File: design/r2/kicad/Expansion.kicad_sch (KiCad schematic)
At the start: 29 parts, among them IC1 MC68010P10, IC7 74LS148, J3 Conn_02x32_Odd_Even, J5 PWR, J6 Conn_01x04_Male

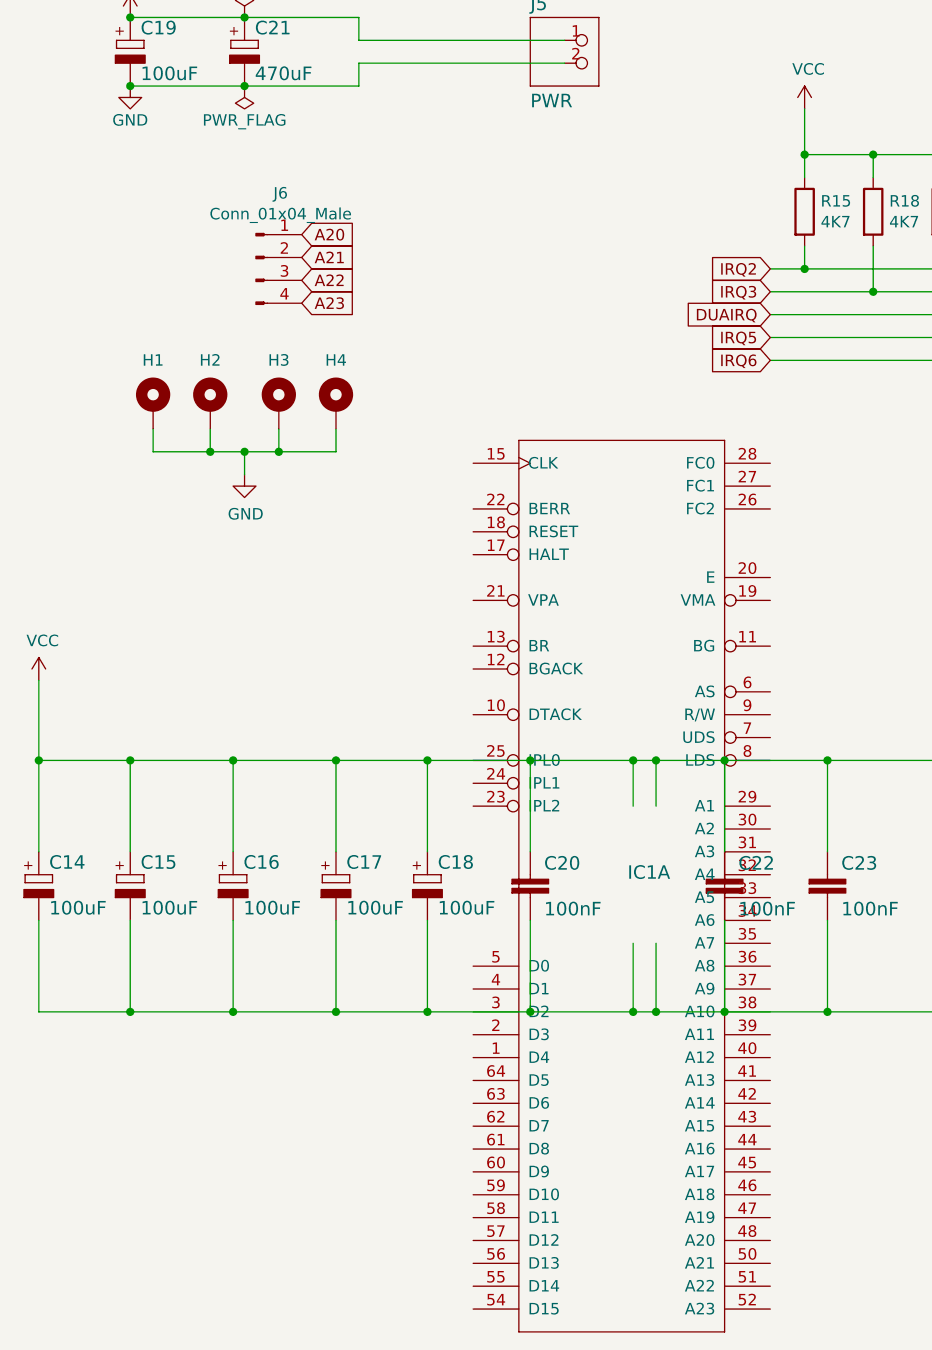
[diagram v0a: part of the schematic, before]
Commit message: Fix #333 (partial) and #307
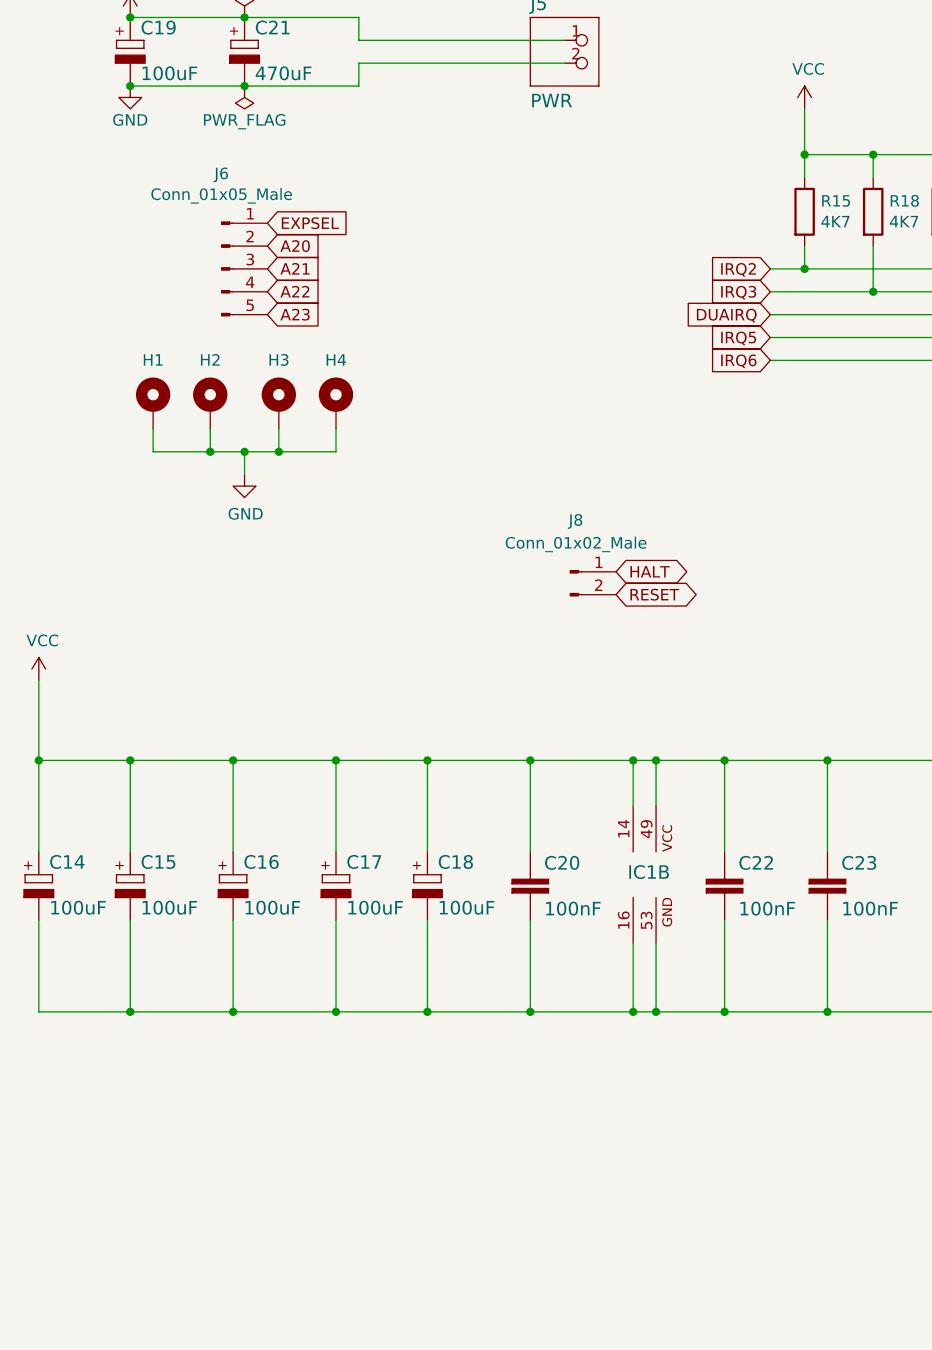
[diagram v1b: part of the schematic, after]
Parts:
- added J8: Conn_01x02_Male, Connector_PinHeader_2.54mm:PinHeader_1x02_P2.54mm_Vertical, symbol Connector:Conn_01x02_Male
- J6: value Conn_01x04_Male -> Conn_01x05_Male; footprint Connector_PinHeader_2.54mm:PinHeader_1x04_P2.54mm_Vertical -> Connector_PinHeader_2.54mm:PinHeader_1x05_P2.54mm_Vertical; symbol Connector:Conn_01x04_Male -> Connector:Conn_01x05_Male
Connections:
- net A20: now also J6.2 (Pin_2); no longer J6.1 (Pin_1)
- net A21: now also J6.3 (Pin_3); no longer J6.2 (Pin_2)
- net A22: now also J6.4 (Pin_4); no longer J6.3 (Pin_3)
- net A23: now also J6.5 (Pin_5); no longer J6.4 (Pin_4)
- net EXPSEL: now also J6.1 (Pin_1)
- net GND: now also IC1.16 (GND@1), IC1.53 (GND@2)
- net RESET: now also J8.2 (Pin_2)
- net VCC: now also IC1.14 (VCC@1), IC1.49 (VCC@2)
- new net HALT: J8.1 (Pin_1)
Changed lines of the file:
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@@
   (title_block
     (title "ROSCO_M68K GENERAL PURPOSE MC68010 COMPUTER")
-    (date "2022-01-14")
-    (rev "2.12")
+    (date "2023-08-17")
+    (rev "2.13-DEV")
     (company "The Really Old-School Company Limited")
     (comment 1 "OSHWA UK000006 (https://certification.oshwa.org/uk000006.html)")
     (comment 2 "See https://github.com/roscopeco/rosco_m68k/blob/master/LICENCE.hardware.txt")
     (comment 3 "Open Source Hardware licenced under CERN Open Hardware Licence")
-    (comment 4 "Copyright 2019-2022 Ross Bamford and Contributors")
+    (comment 4 "Copyright 2019-2023 Ross Bamford and Contributors")
   )
   (junction (at 38.1 83.82) (diameter 0) (color 0 0 0 0)
@@
     )
   )
-  (global_label "A21" (shape input) (at 48.26 62.23 0) (fields_autoplaced)
-    (effects (font (size 1.27 1.27)) (justify left))
-    (property "Intersheet References" "${INTERSHEET_REFS}" (id 0) (at 0 0 0)
-      (effects (font (size 1.27 1.27)) hide)
+  (global_label "A21" (shape input) (at 44.45 63.5 0) (fields_autoplaced)
+    (effects (font (size 1.27 1.27)) (justify left))
+    (property "Intersheet References" "${INTERSHEET_REFS}" (id 0) (at -3.81 1.27 0)
+      (effects (font (size 1.27 1.27)) hide)
+    )
+  )
+  (global_label "EXPSEL" (shape input) (at 44.45 58.42 0) (fields_autoplaced)
+    (effects (font (size 1.27 1.27)) (justify left))
+    (property "Intersheet References" "${INTERSHEET_REFS}" (id 0) (at 53.7894 58.3406 0)
+      (effects (font (size 1.27 1.27)) (justify left) hide)
+    )
+  )
+  (global_label "RESET" (shape tri_state) (at 83.185 99.695 0) (fields_autoplaced)
+    (effects (font (size 1.27 1.27)) (justify left))
+    (property "Intersheet References" "${INTERSHEET_REFS}" (id 0) (at 91.2544 99.6156 0)
+      (effects (font (size 1.27 1.27)) (justify left) hide)
     )
   )
@@
     )
   )
-  (global_label "A20" (shape input) (at 48.26 59.69 0) (fields_autoplaced)
-    (effects (font (size 1.27 1.27)) (justify left))
-    (property "Intersheet References" "${INTERSHEET_REFS}" (id 0) (at 0 0 0)
+  (global_label "A20" (shape input) (at 44.45 60.96 0) (fields_autoplaced)
+    (effects (font (size 1.27 1.27)) (justify left))
+    (property "Intersheet References" "${INTERSHEET_REFS}" (id 0) (at -3.81 1.27 0)
       (effects (font (size 1.27 1.27)) hide)
     )
@@
     )
   )
-  (global_label "A22" (shape input) (at 48.26 64.77 0) (fields_autoplaced)
-    (effects (font (size 1.27 1.27)) (justify left))
-    (property "Intersheet References" "${INTERSHEET_REFS}" (id 0) (at 0 0 0)
+  (global_label "A22" (shape input) (at 44.45 66.04 0) (fields_autoplaced)
+    (effects (font (size 1.27 1.27)) (justify left))
+    (property "Intersheet References" "${INTERSHEET_REFS}" (id 0) (at -3.81 1.27 0)
       (effects (font (size 1.27 1.27)) hide)
     )
@@
     )
   )
+  (global_label "HALT" (shape tri_state) (at 83.185 97.155 0) (fields_autoplaced)
+    (effects (font (size 1.27 1.27)) (justify left))
+    (property "Intersheet References" "${INTERSHEET_REFS}" (id 0) (at 89.924 97.0756 0)
+      (effects (font (size 1.27 1.27)) (justify left) hide)
+    )
+  )
   (global_label "A23" (shape input) (at 214.63 99.06 180) (fields_autoplaced)
     (effects (font (size 1.27 1.27)) (justify right))
@@
     )
   )
-  (global_label "A23" (shape input) (at 48.26 67.31 0) (fields_autoplaced)
-    (effects (font (size 1.27 1.27)) (justify left))
-    (property "Intersheet References" "${INTERSHEET_REFS}" (id 0) (at 0 0 0)
+  (global_label "A23" (shape input) (at 44.45 68.58 0) (fields_autoplaced)
+    (effects (font (size 1.27 1.27)) (justify left))
+    (property "Intersheet References" "${INTERSHEET_REFS}" (id 0) (at -3.81 1.27 0)
       (effects (font (size 1.27 1.27)) hide)
     )
@@
     (pin "2")
   )
-  (symbol (lib_id "rosco_m68k-eagle-import:MC68000P") (at 85.09 130.81 0) (unit 1)
+  (symbol (lib_id "rosco_m68k-eagle-import:MC68000P") (at 85.09 130.81 0) (unit 2)
     (in_bom yes) (on_board yes)
     (property "Reference" "IC1" (id 0) (at 84.455 131.445 0)
@@
       (effects (font (size 1.27 1.27)) hide)
     )
-    (pin "1")
-    (pin "10")
-    (pin "11")
-    (pin "12")
-    (pin "13")
-    (pin "15")
-    (pin "17")
-    (pin "18")
-    (pin "19")
-    (pin "2")
-    (pin "20")
-    (pin "21")
-    (pin "22")
-    (pin "23")
-    (pin "24")
-    (pin "25")
-    (pin "26")
-    (pin "27")
-    (pin "28")
-    (pin "29")
-    (pin "3")
-    (pin "30")
-    (pin "31")
-    (pin "32")
-    (pin "33")
-    (pin "34")
-    (pin "35")
-    (pin "36")
-    (pin "37")
-    (pin "38")
-    (pin "39")
-    (pin "4")
-    (pin "40")
-    (pin "41")
-    (pin "42")
-    (pin "43")
-    (pin "44")
-    (pin "45")
-    (pin "46")
-    (pin "47")
-    (pin "48")
-    (pin "5")
-    (pin "50")
-    (pin "51")
-    (pin "52")
-    (pin "54")
-    (pin "55")
-    (pin "56")
-    (pin "57")
-    (pin "58")
-    (pin "59")
-    (pin "6")
-    (pin "60")
-    (pin "61")
-    (pin "62")
-    (pin "63")
-    (pin "64")
-    (pin "7")
-    (pin "8")
-    (pin "9")
+    (pin "14")
+    (pin "16")
+    (pin "49")
+    (pin "53")
   )
   (symbol (lib_id "rosco_m68k-eagle-import:C2,5-3") (at 73.66 130.81 0) (unit 1)
@@
     (pin "2")
   )
-  (symbol (lib_id "Connector:Conn_01x04_Male") (at 43.18 62.23 0) (unit 1)
-    (in_bom yes) (on_board yes)
-    (property "Reference" "J6" (id 0) (at 45.9232 55.0926 0))
-    (property "Value" "Conn_01x04_Male" (id 1) (at 45.9232 57.404 0))
-    (property "Footprint" "Connector_PinHeader_2.54mm:PinHeader_1x04_P2.54mm_Vertical" (id 2) (at 43.18 62.23 0)
-      (effects (font (size 1.27 1.27)) hide)
-    )
-    (property "Datasheet" "~" (id 3) (at 43.18 62.23 0)
+  (symbol (lib_id "Connector:Conn_01x05_Male") (at 39.37 63.5 0) (unit 1)
+    (in_bom yes) (on_board yes)
+    (property "Reference" "J6" (id 0) (at 39.37 52.9336 0))
+    (property "Value" "Conn_01x05_Male" (id 1) (at 39.37 55.245 0))
+    (property "Footprint" "Connector_PinHeader_2.54mm:PinHeader_1x05_P2.54mm_Vertical" (id 2) (at 39.37 63.5 0)
+      (effects (font (size 1.27 1.27)) hide)
+    )
+    (property "Datasheet" "~" (id 3) (at 39.37 63.5 0)
       (effects (font (size 1.27 1.27)) hide)
     )
@@
     (pin "3")
     (pin "4")
+    (pin "5")
   )
   (symbol (lib_id "74xx:74LS148") (at 161.29 68.58 0) (unit 1)
@@
     (pin "1")
   )
+  (symbol (lib_id "Connector:Conn_01x02_Male") (at 78.105 97.155 0) (unit 1)
+    (in_bom yes) (on_board yes) (fields_autoplaced)
+    (property "Reference" "J8" (id 0) (at 78.74 91.44 0))
+    (property "Value" "Conn_01x02_Male" (id 1) (at 78.74 93.98 0))
+    (property "Footprint" "Connector_PinHeader_2.54mm:PinHeader_1x02_P2.54mm_Vertical" (id 2) (at 78.105 97.155 0)
+      (effects (font (size 1.27 1.27)) hide)
+    )
+    (property "Datasheet" "~" (id 3) (at 78.105 97.155 0)
+      (effects (font (size 1.27 1.27)) hide)
+    )
+    (pin "1")
+    (pin "2")
+  )
 )

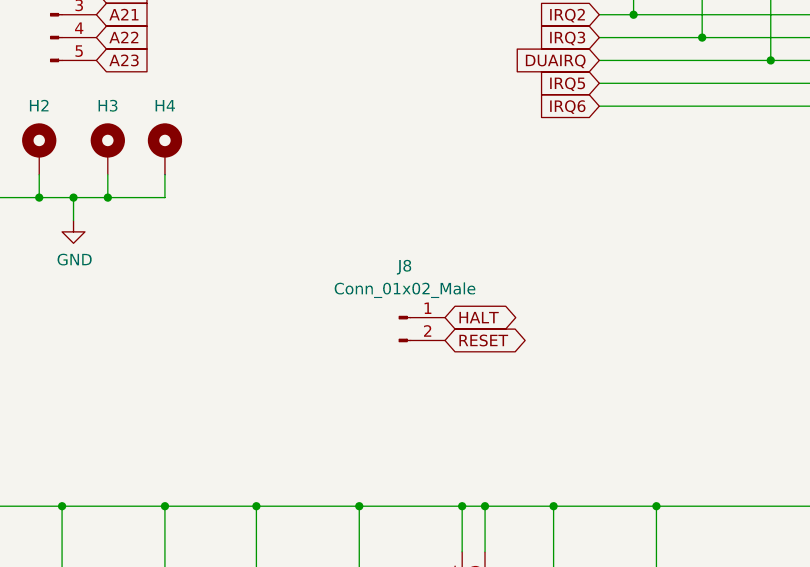
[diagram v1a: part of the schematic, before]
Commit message: Feature/kicad 7 (#388)
* Update r2 to Kicad 7
* Update r2020 to Kicad 7
* Complete Kicad 7 migration
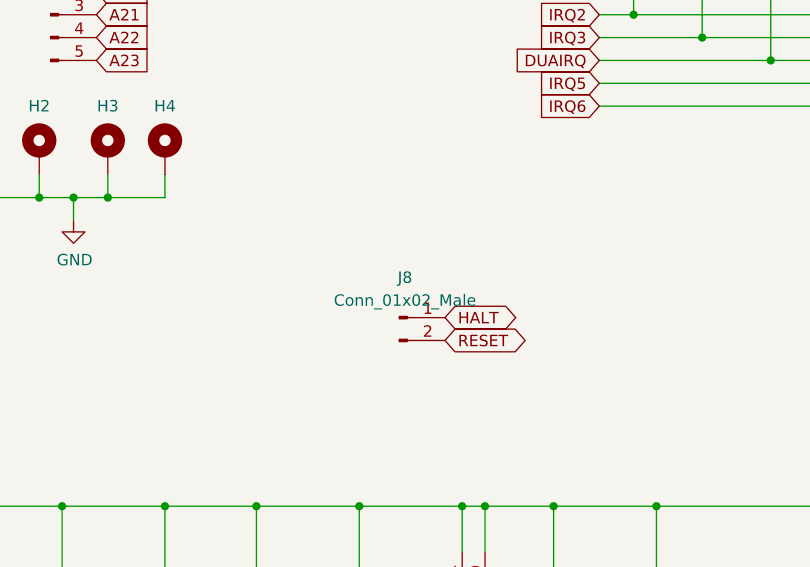
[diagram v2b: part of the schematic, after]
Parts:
- J6: symbol Connector:Conn_01x05_Male -> Connector:Conn_01x05_Pin
- J8: symbol Connector:Conn_01x02_Male -> Connector:Conn_01x02_Pin

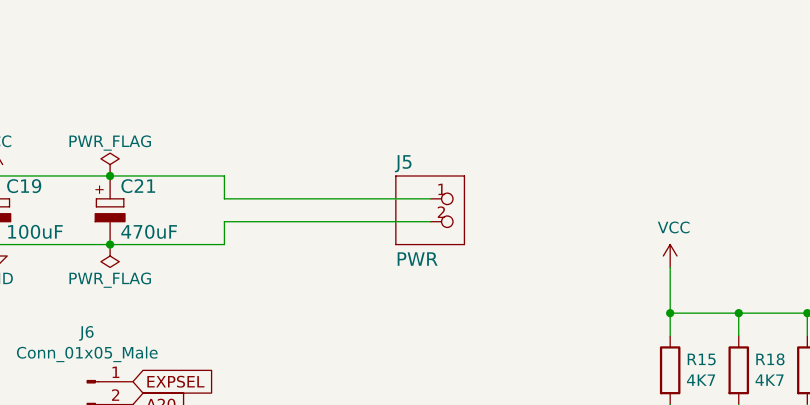
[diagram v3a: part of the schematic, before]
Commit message: Minor classic refresh for 2024 (#416)
* Minor classic refresh for 2024

* Add DC jack
* Silk cleanup
* Unify added memory expansion headers
* Minor routing cleanup
* QR code on silk

* Fix 2020 missing polarity symbol
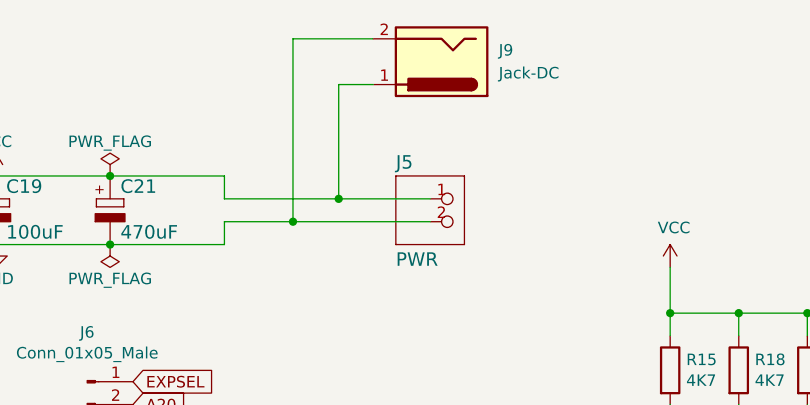
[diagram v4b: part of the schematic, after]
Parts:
- added J9: Jack-DC, Connector_BarrelJack:BarrelJack_Horizontal, symbol Connector:Jack-DC
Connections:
- net GND: now also J9.2
- net VCC: now also J9.1
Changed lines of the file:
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@@
   (title_block
     (title "ROSCO_M68K GENERAL PURPOSE MC68010 COMPUTER")
-    (date "2023-12-10")
-    (rev "2.13-DEV")
+    (date "2024-03-09")
+    (rev "2.2")
     (company "The Really Old-School Company Limited")
     (comment 1 "OSHWA UK000006 (https://certification.oshwa.org/uk000006.html)")
     (comment 2 "See https://github.com/roscopeco/rosco_m68k/blob/master/LICENCE.hardware.txt")
     (comment 3 "Open Source Hardware licenced under CERN Open Hardware Licence")
-    (comment 4 "Copyright 2019-2023 Ross Bamford and Contributors")
+    (comment 4 "Copyright 2019-2024 Ross Bamford and Contributors")
   )
   (junction (at 38.1 83.82) (diameter 0) (color 0 0 0 0)
@@
   (junction (at 111.76 50.8) (diameter 0) (color 0 0 0 0)
   )
+  (junction (at 62.23 40.64) (diameter 0) (color 0 0 0 0)
+  )
   (junction (at 173.99 146.05) (diameter 0) (color 0 0 0 0)
   )
@@
   )
   (junction (at 45.72 83.82) (diameter 0) (color 0 0 0 0)
+  )
+  (junction (at 67.31 38.1) (diameter 0) (color 0 0 0 0)
   )
   (junction (at 139.7 146.05) (diameter 0) (color 0 0 0 0)
@@
     (stroke (width 0) (type default))
   )
+  (wire (pts (xy 62.23 40.64) (xy 54.61 40.64))
+    (stroke (width 0) (type default))
+  )
   (wire (pts (xy 19.05 146.05) (xy 29.21 146.05))
     (stroke (width 0) (type default))
@@
     (stroke (width 0) (type default))
   )
+  (wire (pts (xy 71.12 20.32) (xy 62.23 20.32))
+    (stroke (width 0) (type default))
+  )
   (wire (pts (xy 87.63 146.05) (xy 95.25 146.05))
     (stroke (width 0) (type default))
@@
     (stroke (width 0) (type default))
   )
+  (wire (pts (xy 62.23 20.32) (xy 62.23 40.64))
+    (stroke (width 0) (type default))
+  )
   (wire (pts (xy 240.03 27.94) (xy 240.03 43.18))
     (stroke (width 0) (type default))
@@
     (stroke (width 0) (type default))
   )
-  (wire (pts (xy 77.47 38.1) (xy 54.61 38.1))
+  (wire (pts (xy 71.12 25.4) (xy 67.31 25.4))
+    (stroke (width 0) (type default))
+  )
+  (wire (pts (xy 77.47 38.1) (xy 67.31 38.1))
     (stroke (width 0) (type default))
   )
@@
     (stroke (width 0) (type default))
   )
+  (wire (pts (xy 67.31 25.4) (xy 67.31 38.1))
+    (stroke (width 0) (type default))
+  )
   (wire (pts (xy 119.38 50.8) (xy 111.76 50.8))
     (stroke (width 0) (type default))
@@
     (stroke (width 0) (type default))
   )
-  (wire (pts (xy 77.47 40.64) (xy 54.61 40.64))
+  (wire (pts (xy 77.47 40.64) (xy 62.23 40.64))
     (stroke (width 0) (type default))
   )
@@
   )
   (wire (pts (xy 106.68 118.11) (xy 95.25 118.11))
+    (stroke (width 0) (type default))
+  )
+  (wire (pts (xy 67.31 38.1) (xy 54.61 38.1))
     (stroke (width 0) (type default))
   )
@@
         )
       )
+    )
+  )
+  (symbol (lib_id "Connector:Jack-DC") (at 78.74 22.86 180) (unit 1)
+    (in_bom yes) (on_board yes) (dnp no) (fields_autoplaced)
+    (property "Reference" "J9" (at 85.09 21.59 0)
+      (effects (font (size 1.27 1.27)) (justify right))
+    )
+    (property "Value" "Jack-DC" (at 85.09 24.13 0)
+      (effects (font (size 1.27 1.27)) (justify right))
+    )
+    (property "Footprint" "Connector_BarrelJack:BarrelJack_Horizontal" (at 77.47 21.844 0)
+      (effects (font (size 1.27 1.27)) hide)
+    )
+    (property "Datasheet" "~" (at 77.47 21.844 0)
+      (effects (font (size 1.27 1.27)) hide)
+    )
+    (pin "1")
+    (pin "2")
+    (instances
+      (project "rosco_m68k"
+        (path "/9031bb33-c6aa-4758-bf5c-3274ed3ebab7/00000000-0000-0000-0000-00005e53bc83"
+          (reference "J9") (unit 1)
+        )
+      )
+      (project "rosco_6502"
+        (path "/e63e39d7-6ac0-4ffd-8aa3-1841a4541b55"
+          (reference "J7") (unit 1)
+        )
+      )
